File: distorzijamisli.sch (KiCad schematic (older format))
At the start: 89 parts, among them J1 SW DBG, J12 5V, J2 USB_OTG, J3 Conn_02x16_Odd_Even, J4 Conn_02x16_Odd_Even, J5 Conn_02x08_Odd_Even, J6 Conn_02x03_Odd_Even, J7 Conn_02x03_Odd_Even, SW1 SW_Push, U1 STM32F407VGTx, U3 LD3985M30R_SOT23, U4 LD3985M33R_SOT23, X1 8MHz

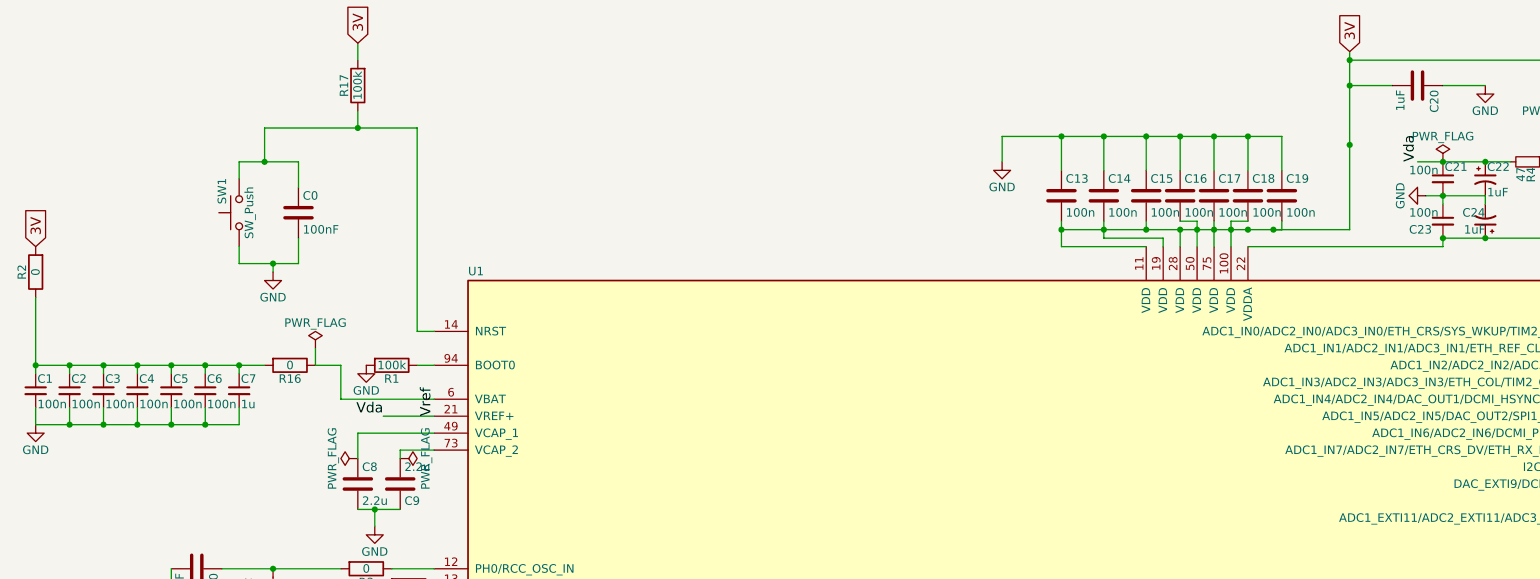
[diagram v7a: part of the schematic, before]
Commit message: Connect Vbat directly to Vdd
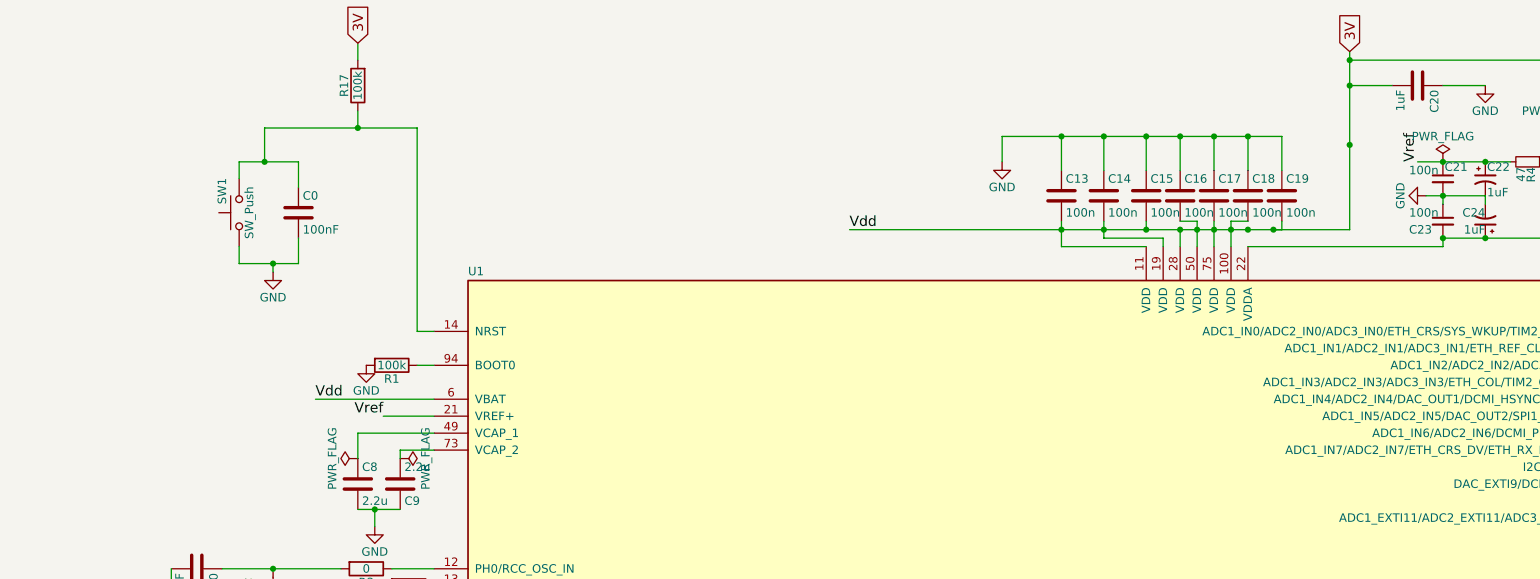
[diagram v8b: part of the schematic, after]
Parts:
- removed C1, C2, C3, C4, C5, C6: 100n, Capacitors_SMD:C_0805_HandSoldering, symbol C_Small
- removed C7: 1u, Capacitors_SMD:C_0805_HandSoldering, symbol C_Small
- removed R16, R2: 0, Resistors_SMD:R_0805_HandSoldering, symbol R
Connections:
- net 3V: now also U1.6 (VBAT)
- net Vda renamed Vref
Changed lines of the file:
@@
-$EndComp
-$Comp
-L GND #PWR03
-U 1 1 59FF689C
-P 650 3100
-F 0 "#PWR03" H 650 2850 50  0001 C CNN
-F 1 "GND" H 650 2950 50  0000 C CNN
-F 2 "" H 650 3100 50  0001 C CNN
-F 3 "" H 650 3100 50  0001 C CNN
-	1    650  3100
-	1    0    0    -1
 $EndComp
 $Comp
@@
 F 3 "" H 15100 3450 50  0001 C CNN
 	1    15100 3450
-	1    0    0    -1
-$EndComp
-$Comp
-L C_Small C1
-U 1 1 5A016C9F
-P 650 2900
-F 0 "C1" H 660 2970 50  0000 L CNN
-F 1 "100n" H 660 2820 50  0000 L CNN
-F 2 "Capacitors_SMD:C_0805_HandSoldering" H 650 2900 50  0001 C CNN
-F 3 "" H 650 2900 50  0001 C CNN
-	1    650  2900
-	1    0    0    -1
-$EndComp
-$Comp
-L C_Small C2
-U 1 1 5A016E22
-P 850 2900
-F 0 "C2" H 860 2970 50  0000 L CNN
-F 1 "100n" H 860 2820 50  0000 L CNN
-F 2 "Capacitors_SMD:C_0805_HandSoldering" H 850 2900 50  0001 C CNN
-F 3 "" H 850 2900 50  0001 C CNN
-	1    850  2900
-	1    0    0    -1
-$EndComp
-$Comp
-L C_Small C3
-U 1 1 5A016E90
-P 1050 2900
-F 0 "C3" H 1060 2970 50  0000 L CNN
-F 1 "100n" H 1060 2820 50  0000 L CNN
-F 2 "Capacitors_SMD:C_0805_HandSoldering" H 1050 2900 50  0001 C CNN
-F 3 "" H 1050 2900 50  0001 C CNN
-	1    1050 2900
-	1    0    0    -1
-$EndComp
-$Comp
-L C_Small C4
-U 1 1 5A016FCA
-P 1250 2900
-F 0 "C4" H 1260 2970 50  0000 L CNN
-F 1 "100n" H 1260 2820 50  0000 L CNN
-F 2 "Capacitors_SMD:C_0805_HandSoldering" H 1250 2900 50  0001 C CNN
-F 3 "" H 1250 2900 50  0001 C CNN
-	1    1250 2900
-	1    0    0    -1
-$EndComp
-$Comp
-L C_Small C5
-U 1 1 5A01703D
-P 1450 2900
-F 0 "C5" H 1460 2970 50  0000 L CNN
-F 1 "100n" H 1460 2820 50  0000 L CNN
-F 2 "Capacitors_SMD:C_0805_HandSoldering" H 1450 2900 50  0001 C CNN
-F 3 "" H 1450 2900 50  0001 C CNN
-	1    1450 2900
-	1    0    0    -1
-$EndComp
-$Comp
-L C_Small C6
-U 1 1 5A0170B3
-P 1650 2900
-F 0 "C6" H 1660 2970 50  0000 L CNN
-F 1 "100n" H 1660 2820 50  0000 L CNN
-F 2 "Capacitors_SMD:C_0805_HandSoldering" H 1650 2900 50  0001 C CNN
-F 3 "" H 1650 2900 50  0001 C CNN
-	1    1650 2900
-	1    0    0    -1
-$EndComp
-$Comp
-L C_Small C7
-U 1 1 5A017155
-P 1850 2900
-F 0 "C7" H 1860 2970 50  0000 L CNN
-F 1 "1u" H 1860 2820 50  0000 L CNN
-F 2 "Capacitors_SMD:C_0805_HandSoldering" H 1850 2900 50  0001 C CNN
-F 3 "" H 1850 2900 50  0001 C CNN
-	1    1850 2900
 	1    0    0    -1
 $EndComp
@@
 Text Label 12950 8400 1    60   ~ 0
 ADC1_IN15
-Text Label 3000 3050 1    60   ~ 0
+Text Label 2700 3050 2    60   ~ 0
 Vref
-Text Label 2700 3050 2    60   ~ 0
-Vda
 Text Label 8800 1550 1    60   ~ 0
-Vda
+Vref
 $Comp
 L PWR_FLAG #FLG020
@@
 Text GLabel 8400 900  1    60   Input ~ 0
 3V
-Text GLabel 650  2050 1    60   Input ~ 0
-3V
 Text GLabel 900  10850 3    60   Output ~ 0
 5V
@@
 	7200 1950 7200 1900
 Wire Wire Line
-	6700 1950 8000 1950
+	5450 1950 8000 1950
 Wire Wire Line
 	7400 1950 7400 2050
@@
 	8400 1100 8650 1100
 Connection ~ 8400 1100
-Wire Wire Line
-	650  2750 2000 2750
-Wire Wire Line
-	2450 2750 2450 2950
-Wire Wire Line
-	2450 2950 3000 2950
 Wire Wire Line
 	8950 1100 9200 1100
@@
 	15100 3300 15100 3150
 Wire Wire Line
-	650  3000 650  3100
-Wire Wire Line
-	650  3100 1850 3100
-Wire Wire Line
-	1850 3100 1850 3000
-Wire Wire Line
-	1650 3000 1650 3100
-Connection ~ 1650 3100
-Wire Wire Line
-	1450 3000 1450 3100
-Connection ~ 1450 3100
-Wire Wire Line
-	1250 3000 1250 3100
-Connection ~ 1250 3100
-Wire Wire Line
-	1050 3000 1050 3100
-Connection ~ 1050 3100
-Wire Wire Line
-	850  3000 850  3100
-Connection ~ 850  3100
-Wire Wire Line
-	1850 2750 1850 2800
-Connection ~ 1850 2750
-Wire Wire Line
-	1650 2800 1650 2750
-Connection ~ 1650 2750
-Wire Wire Line
-	1450 2750 1450 2800
-Connection ~ 1450 2750
-Wire Wire Line
-	1250 2800 1250 2750
-Connection ~ 1250 2750
-Wire Wire Line
-	1050 2800 1050 2750
-Connection ~ 1050 2750
-Wire Wire Line
-	850  2800 850  2750
-Connection ~ 850  2750
-Wire Wire Line
-	650  2350 650  2800
-Wire Wire Line
 	9550 1550 9650 1550
 Wire Wire Line
@@
 Connection ~ 3100 10200
 Connection ~ 3400 10200
-Connection ~ 650  2750
 Wire Wire Line
 	900  9900 900  10850
@@
 	2250 4050 2700 4050
 $Comp
-L R R16
-U 1 1 5A281E71
-P 2150 2750
-F 0 "R16" V 2230 2750 50  0000 C CNN
-F 1 "0" V 2150 2750 50  0000 C CNN
-F 2 "Resistors_SMD:R_0805_HandSoldering" V 2080 2750 50  0001 C CNN
-F 3 "" H 2150 2750 50  0001 C CNN
-	1    2150 2750
-	0    1    1    0
-$EndComp
-Wire Wire Line
-	2300 2750 2450 2750
-$Comp
-L R R2
-U 1 1 5A282B33
-P 650 2200
-F 0 "R2" V 730 2200 50  0000 C CNN
-F 1 "0" V 650 2200 50  0000 C CNN
-F 2 "Resistors_SMD:R_0805_HandSoldering" V 580 2200 50  0001 C CNN
-F 3 "" H 650 2200 50  0001 C CNN
-	1    650  2200
-	-1   0    0    1
-$EndComp
-$Comp
 L C C20
 U 1 1 5A283BBD
@@
 Text GLabel 13700 6750 1    60   Input ~ 0
 3V
-$Comp
-L PWR_FLAG #FLG027
-U 1 1 5A2941D7
-P 2300 2650
-F 0 "#FLG027" H 2300 2725 50  0001 C CNN
-F 1 "PWR_FLAG" H 2300 2800 50  0000 C CNN
-F 2 "" H 2300 2650 50  0001 C CNN
-F 3 "" H 2300 2650 50  0001 C CNN
-	1    2300 2650
-	1    0    0    -1
-$EndComp
-Wire Wire Line
-	2300 2650 2300 2750
+Text Label 5450 1950 0    60   ~ 0
+Vdd
+Wire Wire Line
+	2300 2950 3000 2950
+Text Label 2300 2950 0    60   ~ 0
+Vdd
 $EndSCHEMATC
